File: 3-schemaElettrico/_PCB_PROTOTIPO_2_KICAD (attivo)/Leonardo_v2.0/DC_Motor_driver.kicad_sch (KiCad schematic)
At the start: 1 part, among them U2 74HC238

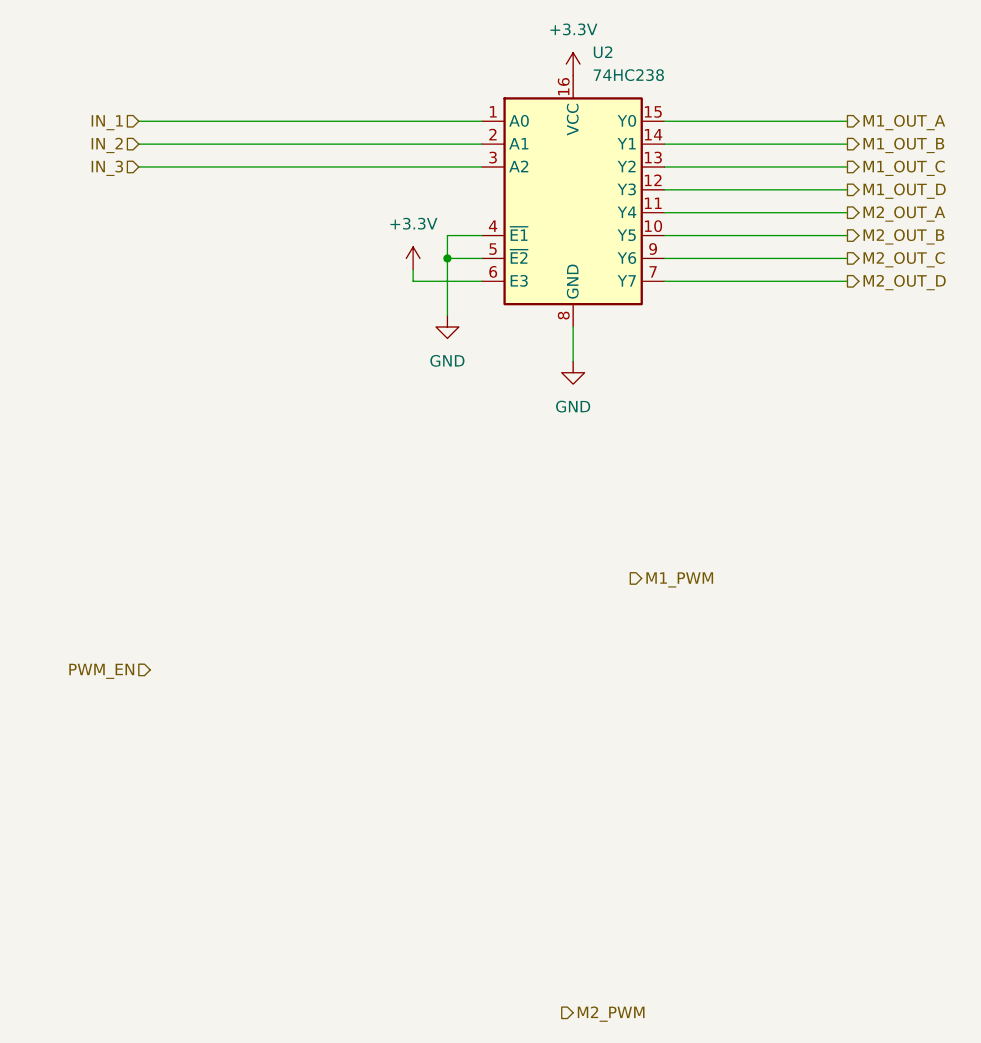
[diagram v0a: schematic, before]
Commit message: placed nodeMCU
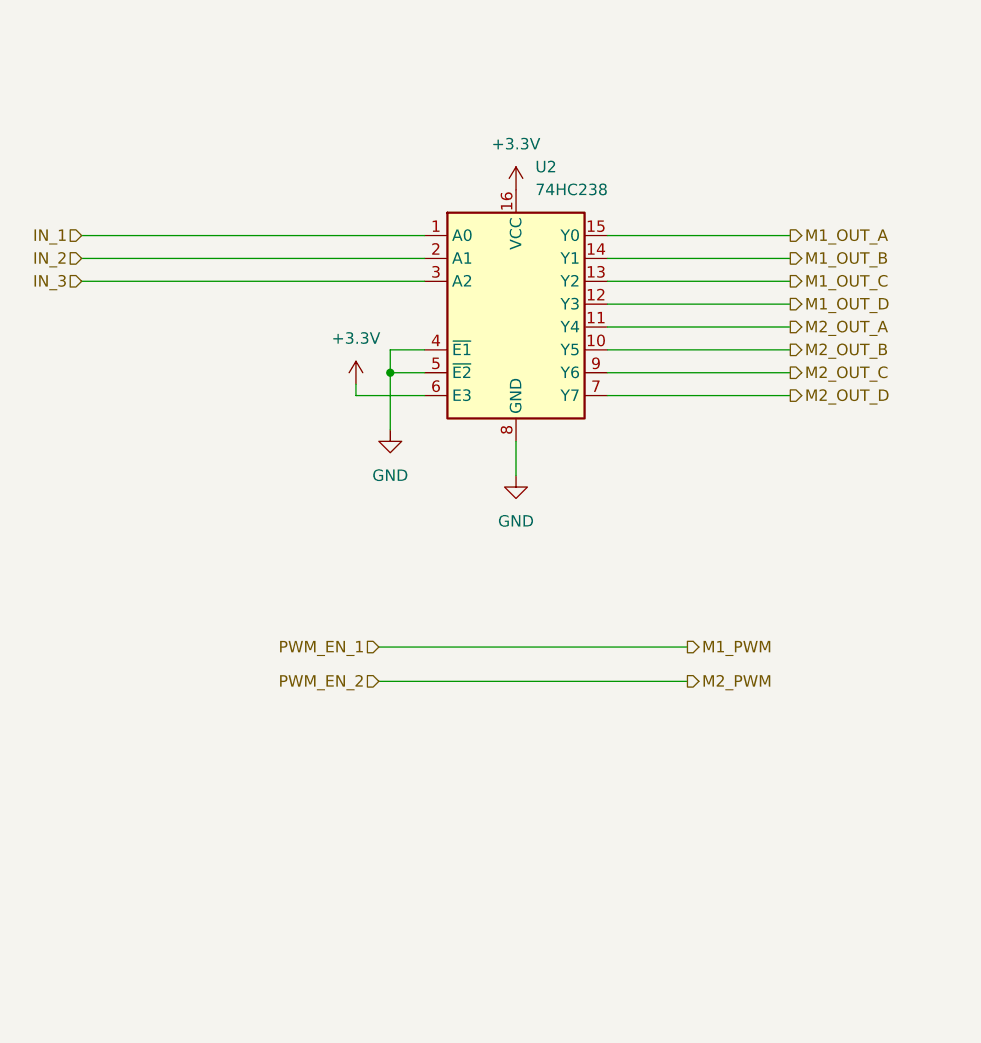
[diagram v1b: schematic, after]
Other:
- moved on the sheet: U2
